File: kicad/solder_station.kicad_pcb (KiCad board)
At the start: 2 copper layers, 28 parts, among them IC1 OPA336U, P1 JACK_2P, P2 POWER, P3 MCU, P4 KEYPAD, SW1 SPST, SW2 SPST, SW3 SPST, SW4 SPST, T1 IRF7416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

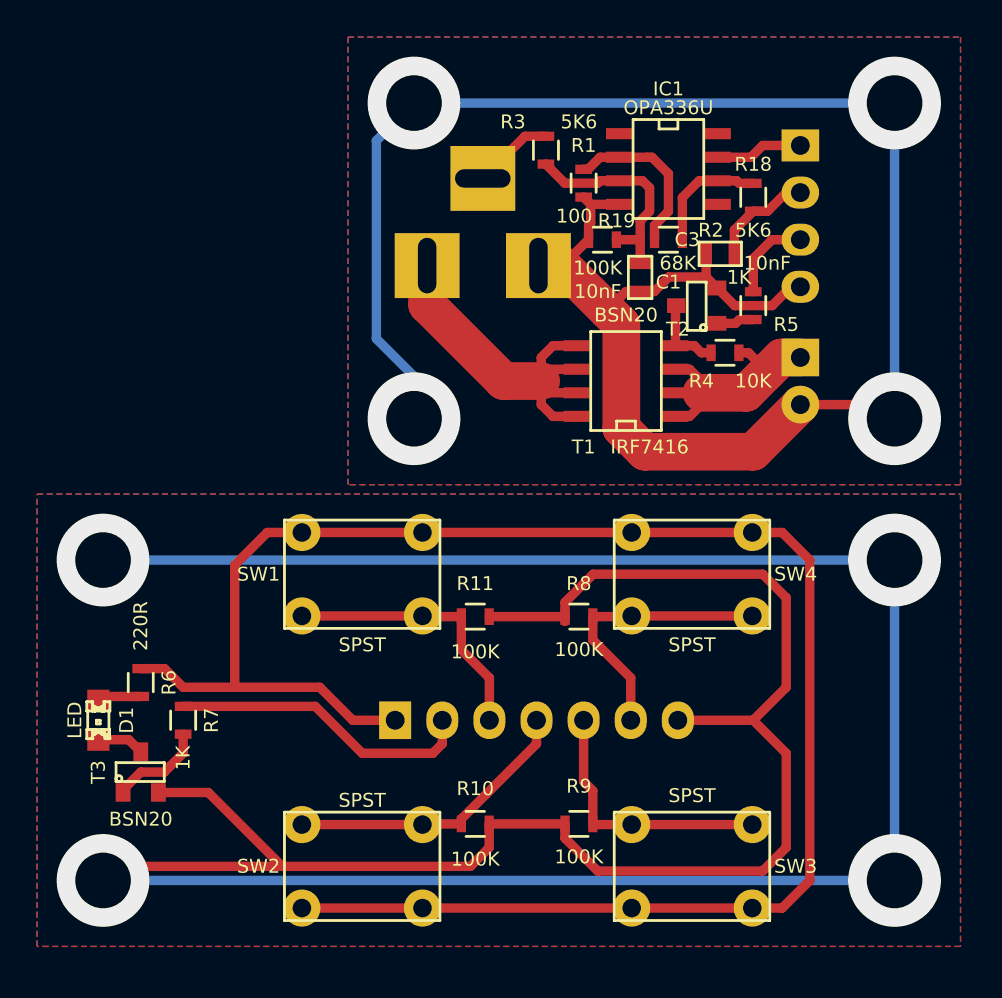
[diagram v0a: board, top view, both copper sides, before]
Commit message: Add arduino nano shield footprint
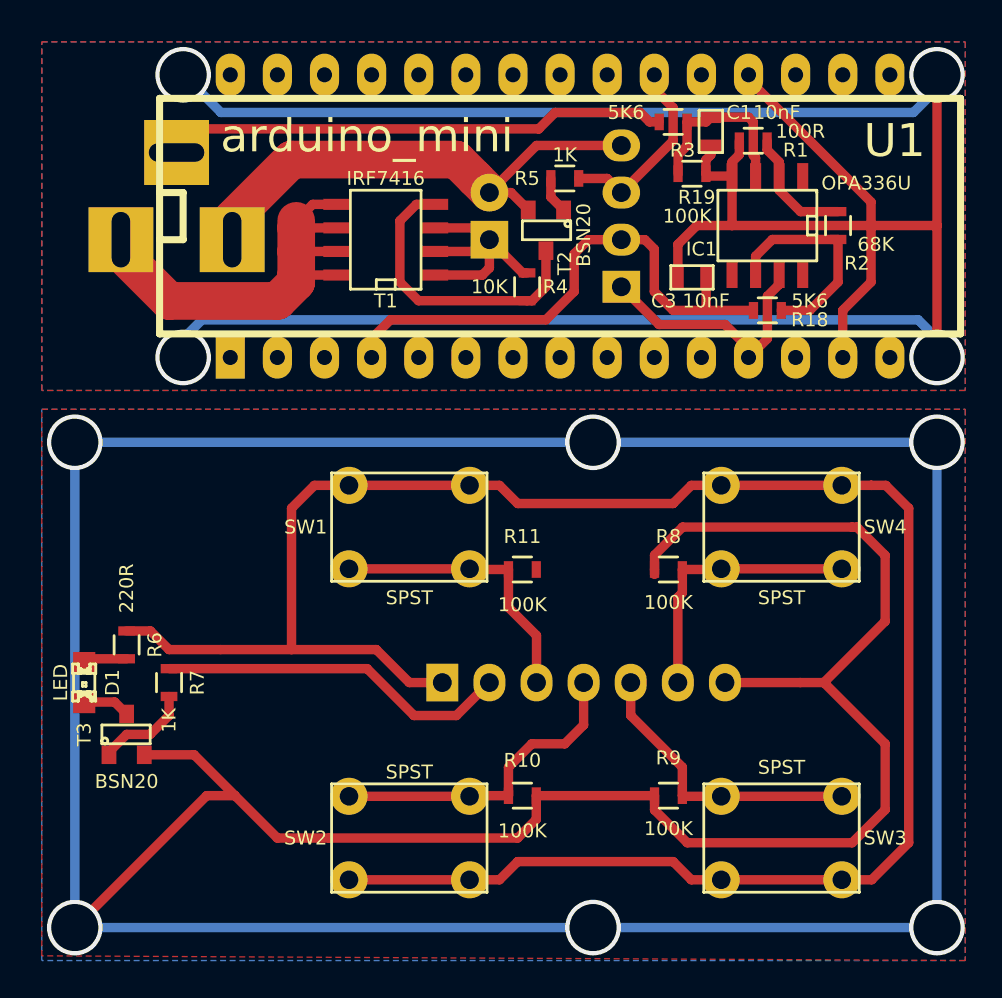
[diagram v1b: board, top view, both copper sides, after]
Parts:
- added U1: arduino_mini, arduino:arduino_mini, F.Cu at (153.4, 95.8)
- R1: value 100 -> 100R
- moved P2 19.0 mm to (148.3, 95.8), turned to 90 degrees
- moved P1 16.6 mm to (128.3, 97.0)
- moved T1 15.0 mm to (142.7, 97.0)
- moved R5 12.3 mm to (152.4, 93.7), turned to 0 degrees
- moved R4 11.2 mm to (150.4, 99.6), turned to 90 degrees
- moved P3 9.65 mm to (155.4, 95.8), turned to 90 degrees
- moved R1 9.43 mm to (162.6, 91.7), turned to 180 degrees
- moved R2 9.18 mm to (167.1, 96.3), turned to 90 degrees
- moved T2 9.09 mm to (151.4, 96.5), turned to 180 degrees
- moved C1 8.75 mm to (160.3, 91.2)
- moved R3 7.03 mm to (158.2, 90.7), turned to 180 degrees
- moved IC1 6.14 mm to (163.3, 96.3), turned to 180 degrees
- moved R18 6.14 mm to (163.3, 100.8), turned to 0 degrees
- moved R19 5.99 mm to (159.3, 93.5), turned to 0 degrees
- moved R8 5.45 mm to (158.0, 114.8)
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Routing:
- net GND: track 110.7 -> 172.4 mm
- net PIN_GND: track 189.0 -> 239.1 mm, vias 4 -> 6
- net MCU_SENSOR: track 5.67 -> 30.0 mm
- net SENSOR: track 4.35 -> 27.1 mm
- net Net-(R4-Pad1): track 4.25 -> 16.1 mm
- net PIN_V+: track 99.1 -> 110.8 mm
- net +5V: track 4.71 -> 13.9 mm
- net MCU_HEATER: track 4.75 -> 10.5 mm
- net Net-(IC1-Pad6): track 6.53 -> 11.8 mm
- net HEATER: track 20.6 -> 24.0 mm
- net PIN_LED: track 16.5 -> 19.1 mm
- net Net-(IC1-Pad2): track 9.07 -> 6.59 mm
- net Net-(C1-Pad1): track 11.8 -> 9.75 mm
- net PIN_B2: track 15.9 -> 17.7 mm
- net PIN_B3: track 14.4 -> 15.9 mm
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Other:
- board text removed: "5V"

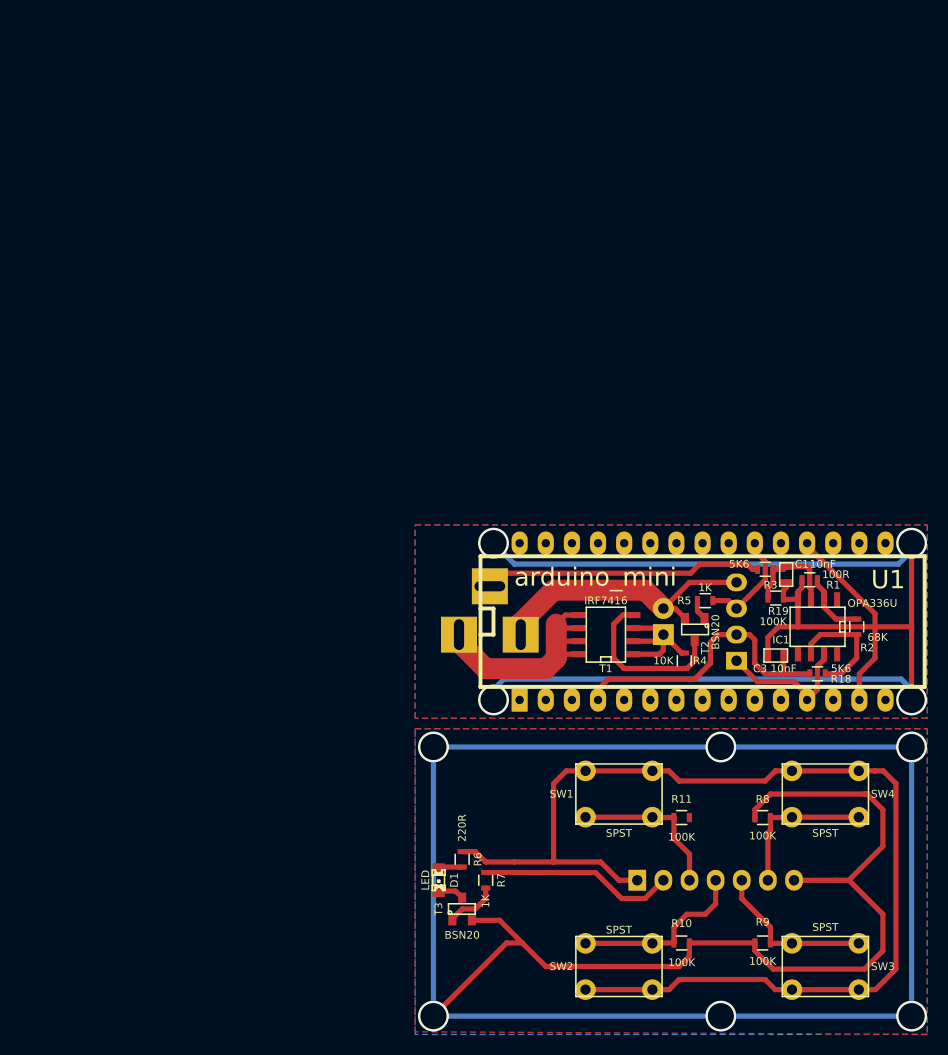
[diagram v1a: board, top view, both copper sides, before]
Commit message: Add Alimentation and connector parts
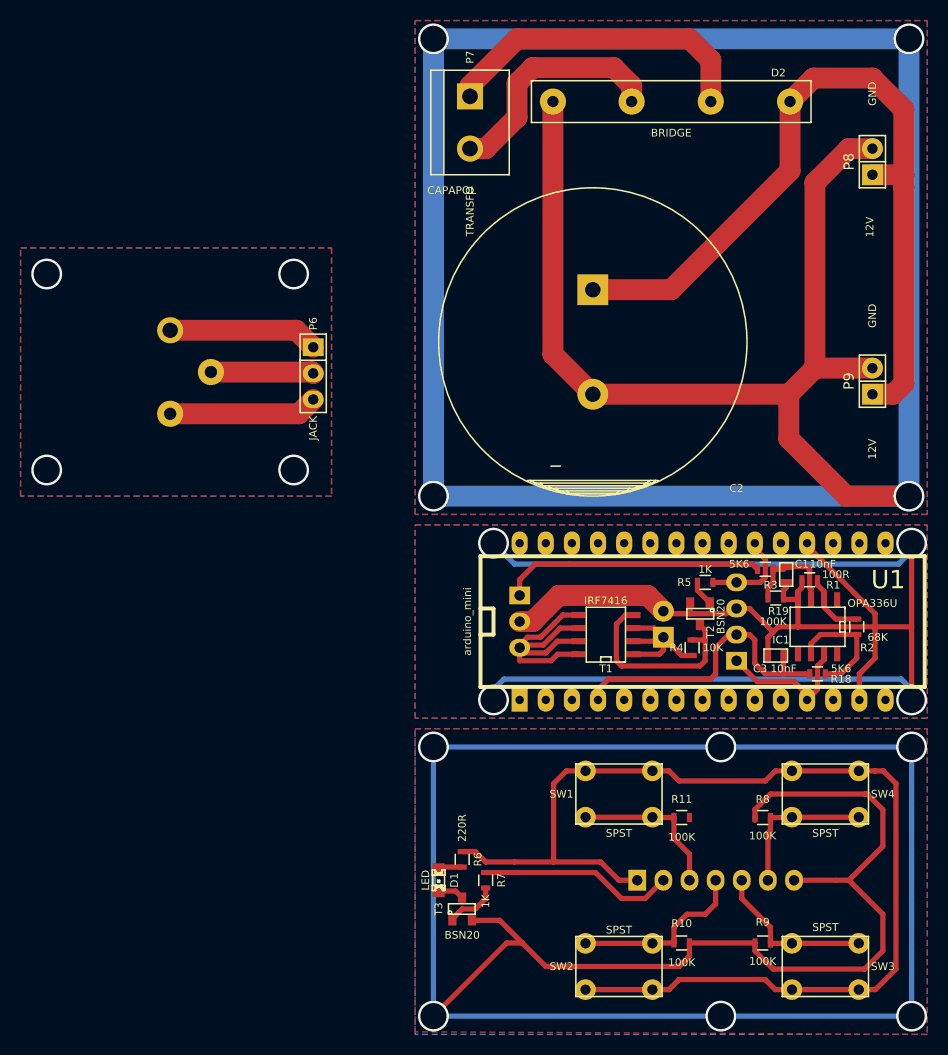
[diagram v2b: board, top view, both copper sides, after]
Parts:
- added C2: CAPAPOL, Capacitors_ThroughHole:Capacitor30x51RM10, F.Cu at (141.5, 68.6)
- added D2: BRIDGE, footprint:DiodeBridge, F.Cu at (149.1, 45.2)
- added P5: JACK, Pin_Headers:Pin_Header_Straight_1x03, B.Cu at (134.4, 95.8)
- added P6: JACK, Pin_Headers:Pin_Header_Straight_1x03, F.Cu at (114.3, 71.6)
- added P7: TRANSFO, Connect:bornier2, F.Cu at (129.5, 47.2)
- added P8: POWER, Pin_Headers:Pin_Header_Straight_1x02, F.Cu at (168.7, 51.1)
- added P9: POWER, Pin_Headers:Pin_Header_Straight_1x02, F.Cu at (168.7, 72.4)
- P1: footprint Connect:BARREL_JACK -> footprint:AC3MMxZV
- moved P1 37.8 mm to (100.4, 71.5), turned to 270 degrees
- moved R5 1.78 mm to (152.4, 91.9)
- moved T2 1.61 mm to (151.9, 95.0)
- moved R4 1.48 mm to (151.1, 98.3), turned to 270 degrees
- moved P2 0.25 mm to (148.3, 96.0)
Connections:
- P1 pad 1: GND -> Net-(P1-Pad1)
- P1 pad 2: HEATER -> Net-(P1-Pad2)
- P1 pad 3: SENSOR -> Net-(P1-Pad3)
- P3 pad 3: MCU_HEATER -> GND
- P3 pad 4: GND -> MCU_HEATER
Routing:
- net Net-(C2-Pad2): track 0.00 -> 282.9 mm, vias 0 -> 4
- net Net-(C2-Pad1): track 0.00 -> 77.1 mm
- net Net-(D2-Pad2): track 0.00 -> 31.2 mm
- net Net-(D2-Pad4): track 0.00 -> 23.2 mm
- net Net-(P1-Pad1): track 0.00 -> 14.6 mm
- net Net-(P1-Pad3): track 0.00 -> 14.5 mm
- net Net-(P1-Pad2): track 0.00 -> 10.4 mm
- net Net-(R4-Pad1): track 16.1 -> 19.6 mm
- net HEATER: track 24.0 -> 27.3 mm
- net SENSOR: track 27.1 -> 25.5 mm
- net GND: track 172.4 -> 173.7 mm
- net (no net): vias 0 -> 4
- added copper zone on B.Cu, net (none)
- added copper zone on F.Cu, net (none)
- added copper zone on B.Cu, net Net-(C2-Pad2)
- added copper zone on F.Cu, net Net-(C2-Pad2)

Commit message: Improve power switch
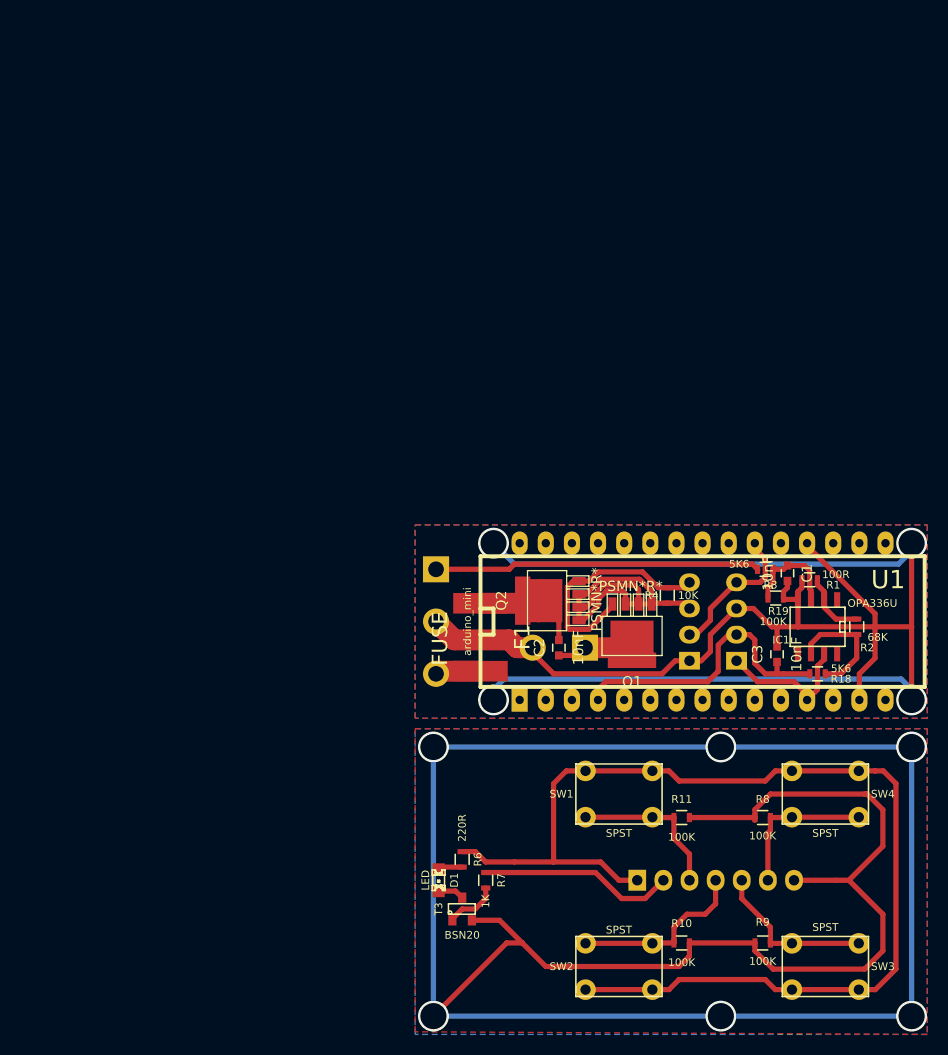
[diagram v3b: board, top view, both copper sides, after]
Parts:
- removed D2: BRIDGE, footprint:DiodeBridge
- removed P1: JACK_2P, footprint:AC3MMxZV
- removed P6: JACK, Pin_Headers:Pin_Header_Straight_1x03
- removed P7: TRANSFO, Connect:bornier2
- removed P8, P9: POWER, Pin_Headers:Pin_Header_Straight_1x02
- removed R5: 1K, Resistors_SMD:R_0603
- removed T1: IRF7416, SMD_Packages:SOIC-8-W
- removed T2: BSN20, SMD_Packages:SOT-23
- added F1: FUSE, footprint:SMD-3121, F.Cu at (130.6, 97.3)
- added Q1: PSMN*R*, footprint:LFPAK-4, F.Cu at (145.3, 96.8)
- added Q2: PSMN*R*, footprint:LFPAK-4, F.Cu at (137.4, 93.7)
- added U2: ROE-0505S, Pin_Headers:Pin_Header_Straight_1x04, B.Cu at (150.9, 99.6)
- C1, C3: footprint SMD_Packages:SMD-0603 -> Capacitors_SMD:C_0603
- C2: value CAPAPOL -> 10nF; footprint Capacitors_ThroughHole:Capacitor30x51RM10 -> Capacitors_SMD:C_0603
- P2: footprint Pin_Headers:Pin_Header_Straight_1x02 -> Connect:bornier2
- P5: footprint Pin_Headers:Pin_Header_Straight_1x03 -> Connect:bornier3
- moved C2 29.9 mm to (138.2, 98.3), turned to 90 degrees
- moved P2 10.4 mm to (138.2, 98.3), turned to 180 degrees
- moved P5 8.13 mm to (126.2, 95.8)
- moved R4 5.62 mm to (148.7, 93.2)
- moved C1 0.18 mm to (160.4, 91.1)
- moved C3 0.18 mm to (159.4, 98.9), turned to 90 degrees
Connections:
- C2 pad 1: Net-(C2-Pad1) -> +12V
- R4 pad 2: +12V -> Net-(Q1-PadS)
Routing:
- net Net-(C2-Pad2): track 282.9 -> 12.3 mm, vias 4 -> 0
- net Net-(C2-Pad1): track 77.1 -> 0.00 mm
- net Net-(Q1-PadS): track 0.00 -> 34.5 mm
- net Net-(D2-Pad2): track 31.2 -> 0.00 mm
- net Net-(D2-Pad4): track 23.2 -> 0.00 mm
- net HEATER: track 27.3 -> 4.42 mm
- net Net-(P1-Pad1): track 14.6 -> 0.00 mm
- net Net-(P1-Pad3): track 14.5 -> 0.00 mm
- net Net-(P1-Pad2): track 10.4 -> 0.00 mm
- net GND: track 173.7 -> 183.5 mm
- net SENSOR: track 25.5 -> 32.4 mm
- net +12V: track 14.3 -> 7.56 mm
- net PIN_GND: track 239.1 -> 245.5 mm
- net MCU_HEATER: track 10.3 -> 16.0 mm
- net Net-(Q1-PadG): track 19.6 -> 22.9 mm
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- removed copper zone on B.Cu, net (none)
- removed copper zone on F.Cu, net (none)
- removed copper zone on B.Cu, net Net-(C2-Pad2)
- removed copper zone on F.Cu, net Net-(C2-Pad2)
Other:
- board text added: "5V"

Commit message: Update kicad project
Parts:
- removed C2: 10nF, Capacitors_SMD:C_0603
- removed Q1, Q2: PSMN*R*, footprint:LFPAK-4
- removed R4: 10K, Resistors_SMD:R_0603
- removed U2: ROE-0505S, Pin_Headers:Pin_Header_Straight_1x04
- added R12: 100K, Resistors_SMD:R_0603, F.Cu at (142.0, 101.1)
- added R13: 10K, Resistors_SMD:R_0603, F.Cu at (145.0, 92.2)
- added T1: BSN20, Diodes_SMD:Diode_SOT23, F.Cu at (147.1, 92.2)
- added T2: IRF7476, SMD_Packages:SOIC-8-N, F.Cu at (139.7, 93.2)
- P3: footprint Pin_Headers:Pin_Header_Straight_1x04 -> Pin_Headers:Pin_Header_Straight_1x05
- P5: footprint Connect:bornier3 -> Connect:bornier4
- T3: footprint SMD_Packages:SOT-23 -> Diodes_SMD:Diode_SOT23
- moved P3 2.62 mm to (156.7, 98.0)
- moved F1 2.40 mm to (131.8, 95.2)
- moved P2 0.92 mm to (138.7, 97.5)
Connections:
- P3 pad 2: MCU_SENSOR -> MCU_STANDBY
- P3 pad 3: GND -> MCU_SENSOR
- P3 pad 4: MCU_HEATER -> GND
- U1 pad 5: Net-(U1-Pad5) -> MCU_STANDBY
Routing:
- net Net-(Q1-PadS): track 34.5 -> 0.00 mm
- net Net-(Q1-PadG): track 22.9 -> 0.00 mm
- net MCU_STANDBY: track 0.00 -> 16.7 mm
- net STANDBY: track 0.00 -> 15.9 mm
- net +12V: track 7.56 -> 20.5 mm
- net Net-(F1-Pad1): track 12.3 -> 22.9 mm
- net MCU_HEATER: track 16.0 -> 23.7 mm
- net GND: track 183.5 -> 190.6 mm
- net Net-(R13-Pad1): track 0.00 -> 4.35 mm
- net MCU_SENSOR: track 29.4 -> 32.8 mm
- net HEATER: track 4.42 -> 5.69 mm
- net +5V: track 13.9 -> 14.6 mm
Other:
- board text added: "SB"

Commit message: Update kicad pcb
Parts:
- D1: footprint LEDs:LED-0805 -> LEDs:LED-5MM
- P4: footprint Pin_Headers:Pin_Header_Straight_1x07 -> footprint:SMT1x7; moved to F.Cu
- moved R6 1.81 mm to (129.9, 117.5)
- moved D1 1.81 mm to (127.6, 119.5)
- moved R7 1.81 mm to (132.2, 119.5)
- moved T3 1.81 mm to (129.9, 122.3)
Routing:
- net PIN_V+: track 110.8 -> 108.6 mm
- net PIN_B3: track 15.9 -> 18.0 mm
- net PIN_B2: track 17.7 -> 15.7 mm
- net PIN_B4: track 14.9 -> 16.4 mm
- net Net-(D1-Pad1): track 2.05 -> 3.27 mm
- net PIN_B1: track 15.3 -> 14.3 mm
- net PIN_LED: track 19.1 -> 18.0 mm
- net PIN_GND: track 245.5 -> 244.7 mm

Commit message: Update circuit
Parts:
- added C2: 100nF, Capacitors_SMD:C_0603, F.Cu at (165.4, 101.0)
- added R5: 1K, Resistors_SMD:R_0603, F.Cu at (146.8, 94.9)
- moved R18 11.0 mm to (153.8, 95.4)
- moved C3 9.69 mm to (150.4, 95.4), turned to 180 degrees
- moved T2 1.14 mm to (148.2, 92.2)
- renumbered R13 to R4, T2 to T1, T1 to T2
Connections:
- T2 pad 1: MCU_HEATER -> Net-(R5-Pad2)
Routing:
- net MCU_SENSOR: track 32.8 -> 20.5 mm
- net Net-(IC1-Pad6): track 11.8 -> 15.2 mm
- net GND: track 190.6 -> 187.5 mm
- net Net-(R5-Pad2): track 0.00 -> 1.69 mm
- net +5V: track 14.6 -> 15.8 mm
- net Net-(R4-Pad1): track 4.35 -> 5.49 mm
